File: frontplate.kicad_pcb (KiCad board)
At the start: 2 copper layers, 200 x 105 mm, 5 parts

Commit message: -
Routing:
- added copper zone on B.Cu, net (none)
- added copper zone on F.Cu, net (none)
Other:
- board text added: "Aktivität"
- board text added: "Temperatur Dach"
- board text added: "Temperatur Keller"
- board text removed: "Herzschlag"
- board text removed: "Temeratur Dach"
- board text removed: "Temeratur Keller"
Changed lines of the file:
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@@
   )
   (setup
-    (last_trace_width 1.5)
+    (last_trace_width 0.25)
     (user_trace_width 0.25)
     (user_trace_width 0.5)
@@
   (gr_circle (center 55.278 61.708) (end 56.878 61.708) (layer Edge.Cuts) (width 0.05))
   (gr_text Manuell/Automatik (at 80.724572 75.819) (layer F.SilkS)
-    (effects (font (size 2 2) (thickness 0.15)))
-  )
-  (gr_text "Temeratur Dach" (at 83.010286 65.4345) (layer F.SilkS)
-    (effects (font (size 2 2) (thickness 0.15)))
-  )
-  (gr_text ∆ϑ1 (at 91.948 70.578) (layer F.SilkS)
-    (effects (font (size 2 2) (thickness 0.15)))
-  )
-  (gr_line (start 95.25 75.819) (end 111.633 75.819) (layer F.SilkS) (width 0.12))
-  (gr_line (start 108.585 70.6755) (end 112.268 66.9925) (layer F.SilkS) (width 0.12))
-  (gr_line (start 95.25 70.6755) (end 108.585 70.6755) (layer F.SilkS) (width 0.12))
-  (gr_line (start 95.25 65.532) (end 100.838 65.532) (layer F.SilkS) (width 0.12))
+    (effects (font (size 2 2) (thickness 0.25)))
+  )
+  (gr_text "Temperatur Dach" (at 81.850381 70.553) (layer F.SilkS)
+    (effects (font (size 2 2) (thickness 0.25)))
+  )
+  (gr_text ∆ϑ1 (at 91.898 65.4095) (layer F.SilkS)
+    (effects (font (size 2 2) (thickness 0.25)))
+  )
+  (gr_line (start 95.25 75.819) (end 111.633 75.819) (layer F.SilkS) (width 0.25))
+  (gr_line (start 108.585 70.6755) (end 112.268 66.9925) (layer F.SilkS) (width 0.25))
+  (gr_line (start 95.25 70.6755) (end 108.585 70.6755) (layer F.SilkS) (width 0.25))
+  (gr_line (start 95.25 65.532) (end 100.838 65.532) (layer F.SilkS) (width 0.25))
   (gr_text EIN/AUS (at 68.082 53.19) (layer F.SilkS)
-    (effects (font (size 2 2) (thickness 0.15)))
-  )
-  (gr_line (start 95.25 102.489) (end 111.633 102.489) (layer F.SilkS) (width 0.12))
-  (gr_line (start 108.585 97.443) (end 112.268 93.76) (layer F.SilkS) (width 0.12))
-  (gr_line (start 95.25 97.443) (end 108.585 97.443) (layer F.SilkS) (width 0.12))
-  (gr_line (start 95.25 92.202) (end 100.838 92.202) (layer F.SilkS) (width 0.12))
+    (effects (font (size 2 2) (thickness 0.25)))
+  )
+  (gr_line (start 95.25 102.489) (end 111.633 102.489) (layer F.SilkS) (width 0.25))
+  (gr_line (start 108.585 97.443) (end 112.268 93.76) (layer F.SilkS) (width 0.25))
+  (gr_line (start 95.25 97.443) (end 108.585 97.443) (layer F.SilkS) (width 0.25))
+  (gr_line (start 95.25 92.202) (end 100.838 92.202) (layer F.SilkS) (width 0.25))
   (gr_text Proportionalanteil (at 80.676952 102.489) (layer F.SilkS)
-    (effects (font (size 2 2) (thickness 0.15)))
-  )
-  (gr_text ∆ϑ2 (at 92.075 97.3455) (layer F.SilkS)
-    (effects (font (size 2 2) (thickness 0.15)))
-  )
-  (gr_text "Temeratur Keller" (at 82.296 92.1045) (layer F.SilkS)
-    (effects (font (size 2 2) (thickness 0.15)))
+    (effects (font (size 2 2) (thickness 0.25)))
+  )
+  (gr_text ∆ϑ2 (at 92.153143 92.0795) (layer F.SilkS)
+    (effects (font (size 2 2) (thickness 0.25)))
+  )
+  (gr_text "Temperatur Keller" (at 80.676952 97.3205) (layer F.SilkS)
+    (effects (font (size 2 2) (thickness 0.25)))
   )
   (gr_text Ein/Aus (at 77.48 136.929) (layer F.SilkS)
-    (effects (font (size 2 2) (thickness 0.15)))
-  )
-  (gr_text Herzschlag (at 114.3 136.929) (layer F.SilkS)
-    (effects (font (size 2 2) (thickness 0.15)))
+    (effects (font (size 2 2) (thickness 0.25)))
+  )
+  (gr_text Aktivität (at 114.3 136.929) (layer F.SilkS)
+    (effects (font (size 2 2) (thickness 0.25)))
   )
   (gr_text Pumpenaktivität (at 204.724 136.929) (layer F.SilkS)
-    (effects (font (size 2 2) (thickness 0.15)))
+    (effects (font (size 2 2) (thickness 0.25)))
   )
   (gr_line (start 156.75 107.061) (end 121.126 107.061) (layer Edge.Cuts) (width 0.05))
@@
   (gr_line (start 238.933 150.208) (end 38.933 150.208) (layer Edge.Cuts) (width 0.05))
   (gr_line (start 238.933 45.208) (end 238.933 150.208) (layer Edge.Cuts) (width 0.05))
+  (zone (net 0) (net_name "") (layer F.Cu) (hatch edge 0.508)
+    (connect_pads (clearance 0.508))
+    (min_thickness 0.254)
+    (fill yes (arc_segments 32) (thermal_gap 0.508) (thermal_bridge_width 0.508))
+    (polygon
+      (pts
+        (xy 239.014 150.241) (xy 38.862 150.241) (xy 38.862 45.085) (xy 239.014 45.085)
+      )
+    )
+  )
+  (zone (net 0) (net_name "") (layer B.Cu) (hatch edge 0.508)
+    (connect_pads (clearance 0.508))
+    (min_thickness 0.254)
+    (fill yes (arc_segments 32) (thermal_gap 0.508) (thermal_bridge_width 0.508))
+    (polygon
+      (pts
+        (xy 239.014 150.241) (xy 38.862 150.241) (xy 38.862 45.085) (xy 239.014 45.085)
+      )
+    )
+  )
 )

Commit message: Production state Rev.B
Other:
- outline, holes or cut-outs redrawn
- board text added: "Reichelt: "SK M3" as nuts (x6)"
- board text added: "Reichelt: "SZK M3X6-200" as screws (x6)"
- board text added: "Reichelt: "VT DA 12MM" as distance bolts (x6)"
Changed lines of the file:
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@@
   (general
     (thickness 1.6)
-    (drawings 65)
+    (drawings 68)
     (tracks 0)
     (zones 0)
@@
   (page A4)
   (layers
-    (0 F.Cu signal)
+    (0 F.Cu signal hide)
     (31 B.Cu signal)
     (32 B.Adhes user hide)
@@
       (drillshape 0)
       (scaleselection 1)
-      (outputdirectory "C:/Users/stoff/source/repos/solaranlage/Production Files/GER/"))
+      (outputdirectory "C:/Users/mstof/source/repos/solaranlage/Production Files/Rev_B/GER/frontpalte"))
   )
   (net 0 "")
@@
     )
   )
+  (gr_text "Reichelt: \"SK M3\" as nuts (x6)" (at 75.820286 182.0545) (layer Eco2.User)
+    (effects (font (size 3 3) (thickness 0.15)))
+  )
+  (gr_text "Reichelt: \"VT DA 12MM\" as distance bolts (x6)" (at 93.748857 177.165) (layer Eco2.User)
+    (effects (font (size 3 3) (thickness 0.15)))
+  )
+  (gr_text "Reichelt: \"SZK M3X6-200\" as screws (x6)" (at 88.963143 171.8945) (layer Eco2.User)
+    (effects (font (size 3 3) (thickness 0.15)))
+  )
   (gr_arc (start 156.75 105.061) (end 156.75 107.061) (angle -90) (layer Edge.Cuts) (width 0.05))
   (gr_arc (start 121.126 105.061) (end 119.126 105.061) (angle -90) (layer Edge.Cuts) (width 0.05))
   (gr_arc (start 156.75 89.63) (end 158.75 89.63) (angle -90) (layer Edge.Cuts) (width 0.05))
-  (gr_arc (start 121.126 89.63) (end 121.126 87.63) (angle -93.6) (layer Edge.Cuts) (width 0.05))
+  (gr_arc (start 121.126 89.63) (end 121.126 87.63) (angle -90) (layer Edge.Cuts) (width 0.05))
   (gr_arc (start 156.75 78.391) (end 156.75 80.391) (angle -90) (layer Edge.Cuts) (width 0.05))
   (gr_arc (start 121.126 78.391) (end 119.126 78.391) (angle -90) (layer Edge.Cuts) (width 0.05))
@@
   (gr_circle (center 222.588 61.708) (end 224.188 61.708) (layer Edge.Cuts) (width 0.05))
   (gr_circle (center 43.433 145.708) (end 45.033 145.708) (layer Edge.Cuts) (width 0.05))
-  (gr_circle (center 55.278 134.216) (end 56.878 134.216) (layer Edge.Cuts) (width 0.05))
+  (gr_circle (center 55.278 133.708) (end 56.878 133.708) (layer Edge.Cuts) (width 0.05))
   (gr_circle (center 43.433 49.708) (end 45.033 49.708) (layer Edge.Cuts) (width 0.05))
   (gr_circle (center 55.278 61.708) (end 56.878 61.708) (layer Edge.Cuts) (width 0.05))
@@
     (connect_pads (clearance 0.508))
     (min_thickness 0.254)
-    (fill yes (arc_segments 32) (thermal_gap 0.508) (thermal_bridge_width 0.508))
+    (fill (arc_segments 32) (thermal_gap 0.508) (thermal_bridge_width 0.508))
     (polygon
       (pts
@@
     (connect_pads (clearance 0.508))
     (min_thickness 0.254)
-    (fill yes (arc_segments 32) (thermal_gap 0.508) (thermal_bridge_width 0.508))
+    (fill (arc_segments 32) (thermal_gap 0.508) (thermal_bridge_width 0.508))
     (polygon
       (pts

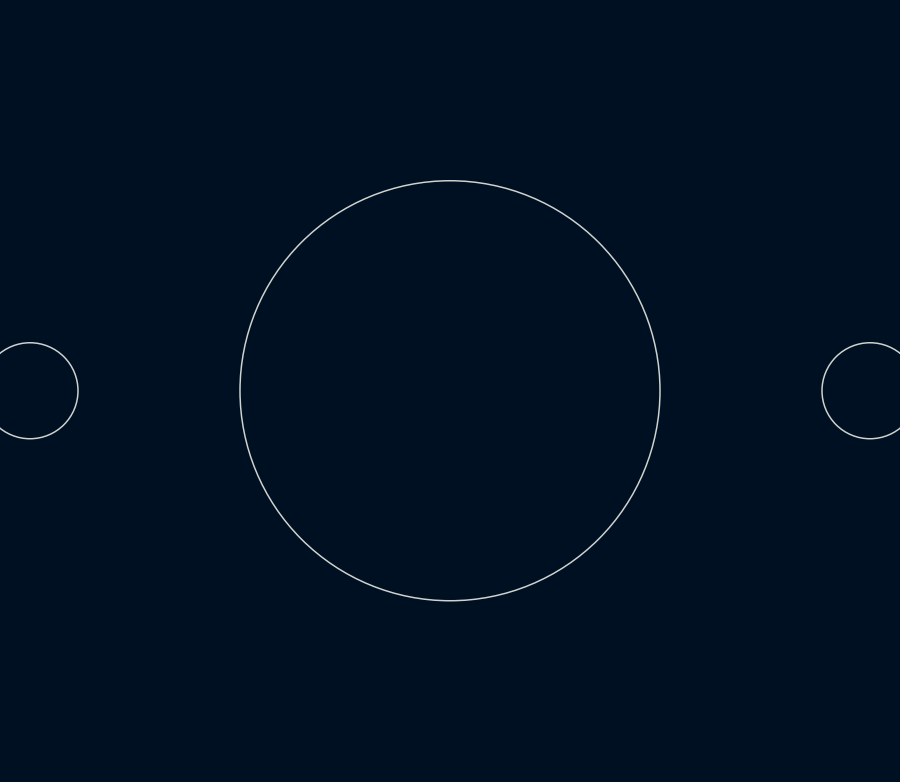
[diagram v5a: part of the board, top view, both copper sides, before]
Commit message: fixes after receiving RevB PCBs: - increased diameter of H6 to 3.2mm; -decrease radius of hole for encoder to 6.5mm
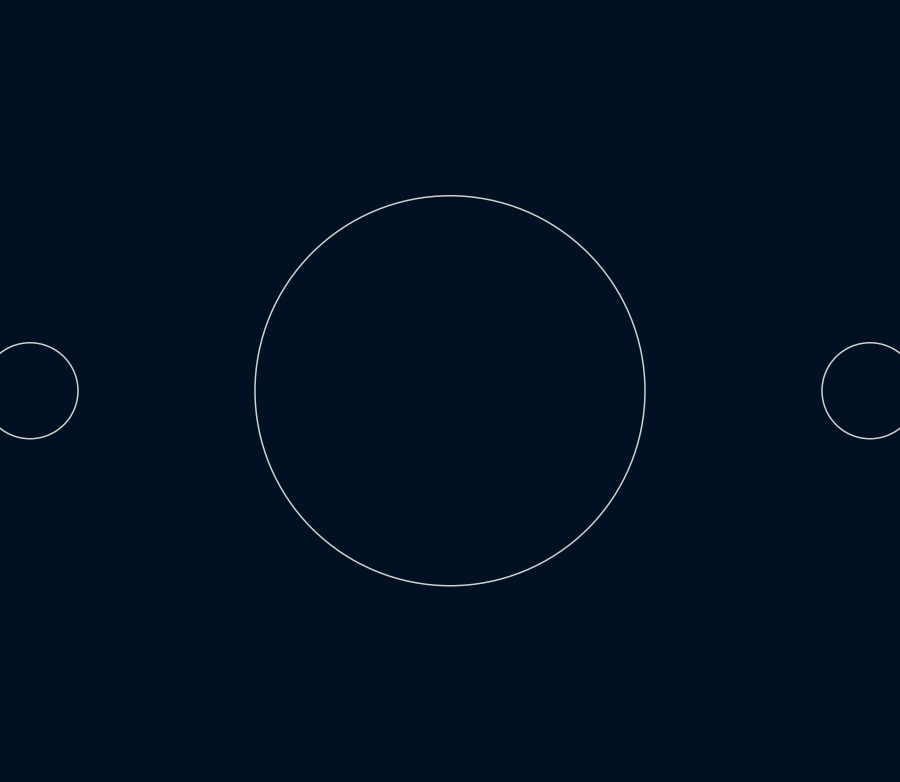
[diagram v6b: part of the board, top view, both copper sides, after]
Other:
- outline, holes or cut-outs redrawn
- board text added: "Reichelt: "SK-E M3-100" as nuts (x6)"
- board text removed: "Reichelt: "SK M3" as nuts (x6)"
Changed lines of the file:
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@@
     )
   )
-  (gr_text "Reichelt: \"SK M3\" as nuts (x6)" (at 75.820286 182.0545) (layer Eco2.User)
+  (gr_text "Reichelt: \"SK-E M3-100\" as nuts (x6)" (at 75.820286 182.0545) (layer Eco2.User)
     (effects (font (size 3 3) (thickness 0.15)))
   )
@@
   (gr_circle (center 114.046 92.202) (end 115.796 92.202) (layer Edge.Cuts) (width 0.05))
   (gr_circle (center 114.173 102.489) (end 115.923 102.489) (layer Edge.Cuts) (width 0.05))
-  (gr_circle (center 139.008 123.413) (end 146.008 123.413) (layer Edge.Cuts) (width 0.05))
+  (gr_circle (center 139.008 123.413) (end 145.508 123.413) (layer Edge.Cuts) (width 0.05))
   (gr_line (start 38.933 45.208) (end 238.933 45.208) (layer Edge.Cuts) (width 0.05))
   (gr_text "200mm x 105mm" (at 60.071 159.639) (layer Eco2.User)
